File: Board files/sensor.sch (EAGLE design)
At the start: 33 parts, among them Q1 BCM847DS, U1 TL974, U2 TL974

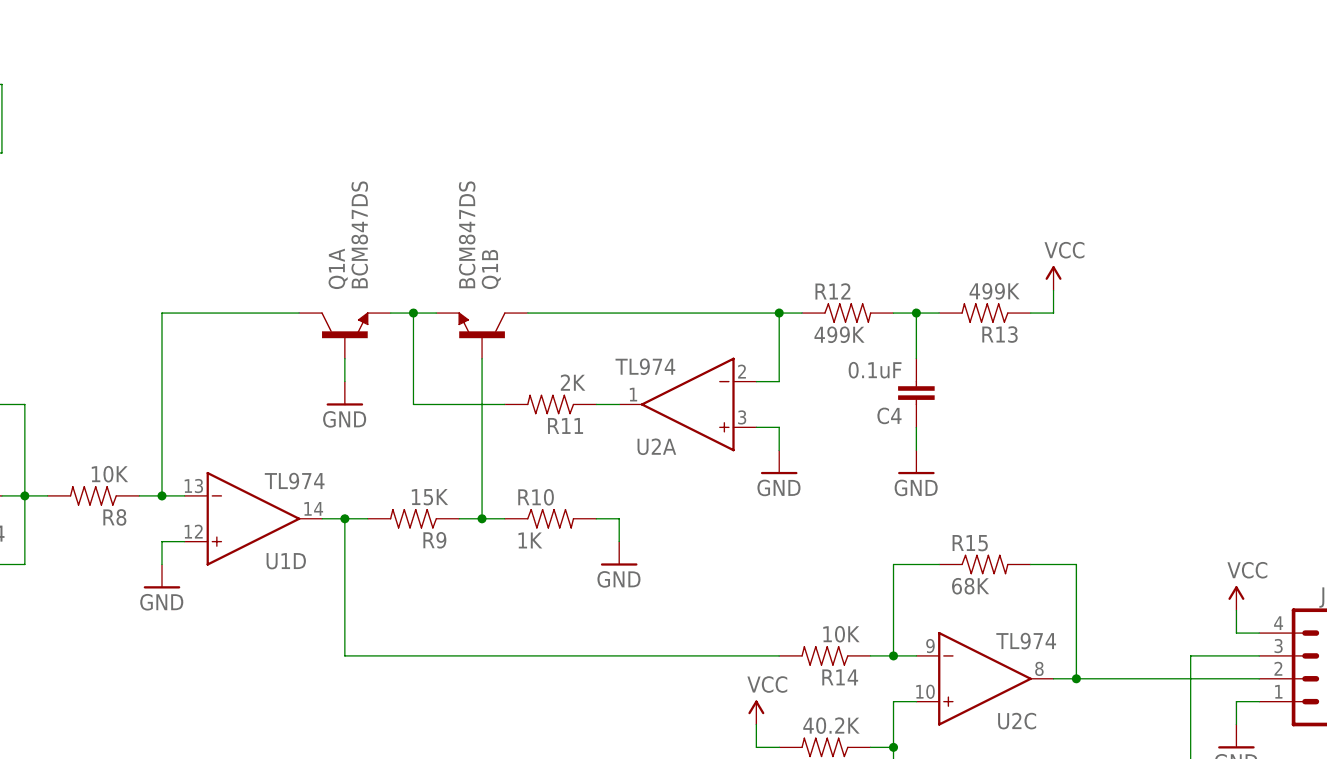
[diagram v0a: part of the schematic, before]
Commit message: Fixed sensor board bug
Added a capacitor between U1p13 and U1p14
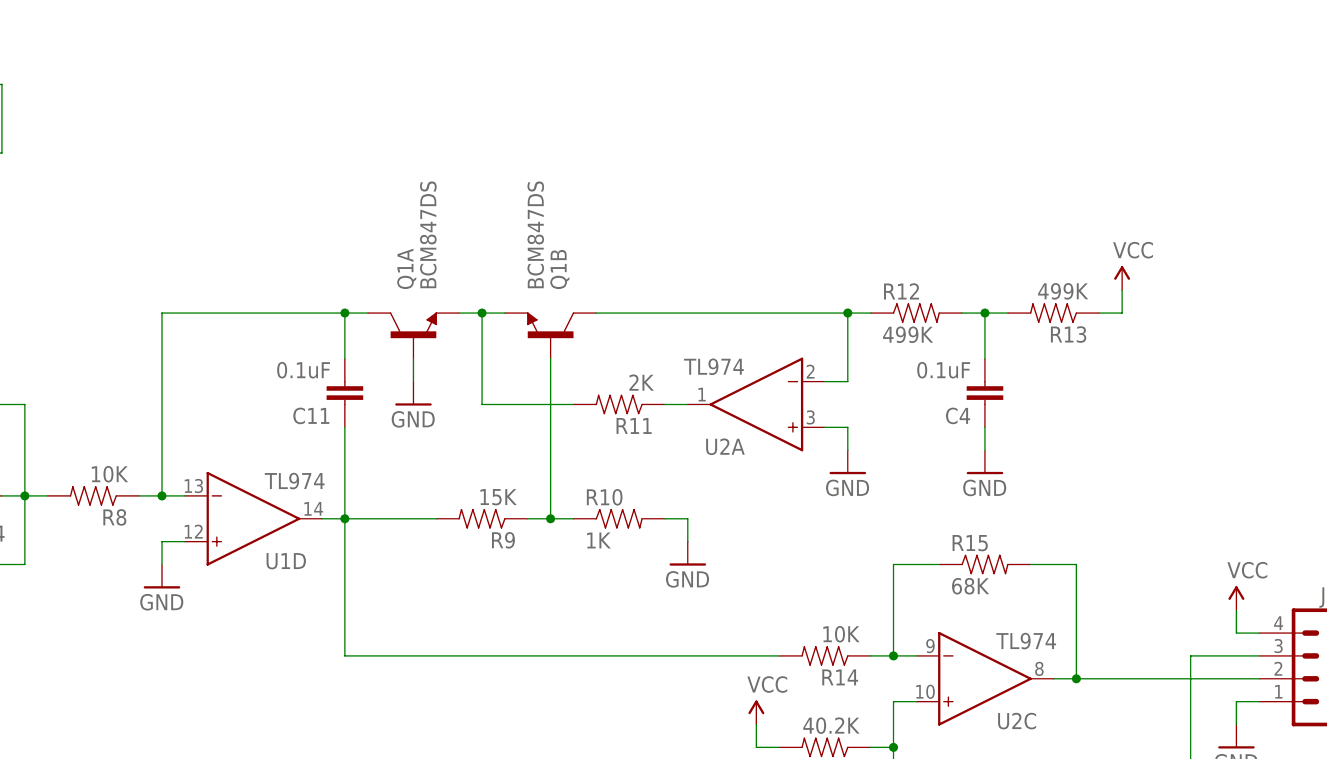
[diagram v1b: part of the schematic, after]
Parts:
- added C11: 0.1uF, SparkFun-Capacitors:CAP0805
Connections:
- net N$13: now also C11.2
- net N$17: now also C11.1
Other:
- moved on the sheet: C4, Q1A, Q1B, R10, R11, R12, R13, R9, U2A
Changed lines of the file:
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@@
 <part name="SUPPLY8" library="SparkFun-Aesthetics" deviceset="VNEG" device=""/>
 <part name="GND16" library="SparkFun-Aesthetics" deviceset="GND" device=""/>
+<part name="C11" library="SparkFun-Capacitors" deviceset="CAP" device="0805" value="0.1uF"/>
 </parts>
 <sheets>
@@
 <instance part="SUPPLY4" gate="G$2" x="17.78" y="86.36"/>
 <instance part="D1" gate="G$1" x="99.06" y="48.26" rot="MR180"/>
-<instance part="Q1" gate="A" x="205.74" y="63.5" rot="R90"/>
-<instance part="Q1" gate="B" x="220.98" y="63.5" rot="MR90"/>
+<instance part="Q1" gate="A" x="213.36" y="63.5" rot="R90"/>
+<instance part="Q1" gate="B" x="228.6" y="63.5" rot="MR90"/>
 <instance part="U1" gate="A" x="50.8" y="40.64"/>
 <instance part="U1" gate="B" x="86.36" y="38.1" rot="MR180"/>
@@
 <instance part="U1" gate="P" x="17.78" y="104.14"/>
 <instance part="U1" gate="D" x="193.04" y="43.18" rot="MR180"/>
-<instance part="U2" gate="A" x="246.38" y="55.88" rot="R180"/>
+<instance part="U2" gate="A" x="254" y="55.88" rot="R180"/>
 <instance part="U2" gate="C" x="274.32" y="25.4" rot="MR180"/>
 <instance part="U2" gate="P" x="53.34" y="104.14"/>
 <instance part="R8" gate="G$1" x="177.8" y="45.72" rot="R180"/>
-<instance part="GND2" gate="1" x="205.74" y="55.88"/>
-<instance part="R9" gate="G$1" x="213.36" y="43.18" rot="R180"/>
-<instance part="R11" gate="G$1" x="228.6" y="55.88" rot="R180"/>
-<instance part="R12" gate="G$1" x="261.62" y="66.04"/>
-<instance part="R10" gate="G$1" x="228.6" y="43.18"/>
-<instance part="GND9" gate="1" x="236.22" y="38.1"/>
-<instance part="GND10" gate="1" x="254" y="48.26"/>
-<instance part="R13" gate="G$1" x="276.86" y="66.04" rot="R180"/>
-<instance part="SUPPLY5" gate="1" x="284.48" y="68.58"/>
-<instance part="C4" gate="G$1" x="269.24" y="58.42" rot="R180"/>
-<instance part="GND11" gate="1" x="269.24" y="48.26"/>
+<instance part="GND2" gate="1" x="213.36" y="55.88"/>
+<instance part="R9" gate="G$1" x="220.98" y="43.18" rot="R180"/>
+<instance part="R11" gate="G$1" x="236.22" y="55.88" rot="R180"/>
+<instance part="R12" gate="G$1" x="269.24" y="66.04"/>
+<instance part="R10" gate="G$1" x="236.22" y="43.18"/>
+<instance part="GND9" gate="1" x="243.84" y="38.1"/>
+<instance part="GND10" gate="1" x="261.62" y="48.26"/>
+<instance part="R13" gate="G$1" x="284.48" y="66.04" rot="R180"/>
+<instance part="SUPPLY5" gate="1" x="292.1" y="68.58"/>
+<instance part="C4" gate="G$1" x="276.86" y="58.42" rot="R180"/>
+<instance part="GND11" gate="1" x="276.86" y="48.26"/>
 <instance part="R14" gate="G$1" x="259.08" y="27.94" rot="R180"/>
 <instance part="R15" gate="G$1" x="276.86" y="38.1"/>
@@
 <instance part="SUPPLY8" gate="G$2" x="104.14" y="86.36"/>
 <instance part="GND16" gate="1" x="116.84" y="96.52"/>
+<instance part="C11" gate="G$1" x="205.74" y="58.42" rot="R180"/>
 </instances>
 <busses>
@@
 <pinref part="Q1" gate="A" pin="B"/>
 <pinref part="GND2" gate="1" pin="GND"/>
-<wire x1="205.74" y1="58.42" x2="205.74" y2="60.96" width="0.1524" layer="91"/>
+<wire x1="213.36" y1="58.42" x2="213.36" y2="60.96" width="0.1524" layer="91"/>
 </segment>
 <segment>
@@
 <segment>
 <pinref part="U2" gate="A" pin="IN+"/>
-<wire x1="251.46" y1="53.34" x2="254" y2="53.34" width="0.1524" layer="91"/>
+<wire x1="259.08" y1="53.34" x2="261.62" y2="53.34" width="0.1524" layer="91"/>
 <pinref part="GND10" gate="1" pin="GND"/>
-<wire x1="254" y1="53.34" x2="254" y2="50.8" width="0.1524" layer="91"/>
+<wire x1="261.62" y1="53.34" x2="261.62" y2="50.8" width="0.1524" layer="91"/>
 </segment>
 <segment>
 <pinref part="C4" gate="G$1" pin="1"/>
 <pinref part="GND11" gate="1" pin="GND"/>
-<wire x1="269.24" y1="50.8" x2="269.24" y2="53.34" width="0.1524" layer="91"/>
+<wire x1="276.86" y1="50.8" x2="276.86" y2="53.34" width="0.1524" layer="91"/>
 </segment>
 <segment>
 <pinref part="GND9" gate="1" pin="GND"/>
 <pinref part="R10" gate="G$1" pin="2"/>
-<wire x1="236.22" y1="40.64" x2="236.22" y2="43.18" width="0.1524" layer="91"/>
-<wire x1="236.22" y1="43.18" x2="233.68" y2="43.18" width="0.1524" layer="91"/>
+<wire x1="243.84" y1="40.64" x2="243.84" y2="43.18" width="0.1524" layer="91"/>
+<wire x1="243.84" y1="43.18" x2="241.3" y2="43.18" width="0.1524" layer="91"/>
 </segment>
 <segment>
@@
 <segment>
 <pinref part="R13" gate="G$1" pin="1"/>
-<wire x1="281.94" y1="66.04" x2="284.48" y2="66.04" width="0.1524" layer="91"/>
+<wire x1="289.56" y1="66.04" x2="292.1" y2="66.04" width="0.1524" layer="91"/>
 <pinref part="SUPPLY5" gate="1" pin="VCC"/>
-<wire x1="284.48" y1="66.04" x2="284.48" y2="68.58" width="0.1524" layer="91"/>
+<wire x1="292.1" y1="66.04" x2="292.1" y2="68.58" width="0.1524" layer="91"/>
 </segment>
 <segment>
@@
 <wire x1="185.42" y1="45.72" x2="182.88" y2="45.72" width="0.1524" layer="91"/>
 <wire x1="185.42" y1="45.72" x2="185.42" y2="66.04" width="0.1524" layer="91"/>
-<wire x1="185.42" y1="66.04" x2="200.66" y2="66.04" width="0.1524" layer="91"/>
+<wire x1="185.42" y1="66.04" x2="205.74" y2="66.04" width="0.1524" layer="91"/>
 <junction x="185.42" y="45.72"/>
+<pinref part="C11" gate="G$1" pin="2"/>
+<wire x1="205.74" y1="66.04" x2="208.28" y2="66.04" width="0.1524" layer="91"/>
+<wire x1="205.74" y1="66.04" x2="205.74" y2="60.96" width="0.1524" layer="91"/>
+<junction x="205.74" y="66.04"/>
 </segment>
 </net>
@@
 <pinref part="Q1" gate="A" pin="E"/>
 <pinref part="Q1" gate="B" pin="E"/>
-<wire x1="215.9" y1="66.04" x2="213.36" y2="66.04" width="0.1524" layer="91"/>
+<wire x1="223.52" y1="66.04" x2="220.98" y2="66.04" width="0.1524" layer="91"/>
 <pinref part="R11" gate="G$1" pin="2"/>
-<wire x1="213.36" y1="66.04" x2="210.82" y2="66.04" width="0.1524" layer="91"/>
-<wire x1="213.36" y1="66.04" x2="213.36" y2="55.88" width="0.1524" layer="91"/>
-<wire x1="213.36" y1="55.88" x2="223.52" y2="55.88" width="0.1524" layer="91"/>
-<junction x="213.36" y="66.04"/>
+<wire x1="220.98" y1="66.04" x2="218.44" y2="66.04" width="0.1524" layer="91"/>
+<wire x1="220.98" y1="66.04" x2="220.98" y2="55.88" width="0.1524" layer="91"/>
+<wire x1="220.98" y1="55.88" x2="231.14" y2="55.88" width="0.1524" layer="91"/>
+<junction x="220.98" y="66.04"/>
 </segment>
 </net>
@@
 <pinref part="R11" gate="G$1" pin="1"/>
 <pinref part="U2" gate="A" pin="OUT"/>
-<wire x1="236.22" y1="55.88" x2="233.68" y2="55.88" width="0.1524" layer="91"/>
+<wire x1="243.84" y1="55.88" x2="241.3" y2="55.88" width="0.1524" layer="91"/>
 </segment>
 </net>
@@
 <pinref part="Q1" gate="B" pin="B"/>
 <pinref part="R9" gate="G$1" pin="1"/>
-<wire x1="220.98" y1="60.96" x2="220.98" y2="43.18" width="0.1524" layer="91"/>
-<wire x1="220.98" y1="43.18" x2="218.44" y2="43.18" width="0.1524" layer="91"/>
+<wire x1="228.6" y1="60.96" x2="228.6" y2="43.18" width="0.1524" layer="91"/>
+<wire x1="228.6" y1="43.18" x2="226.06" y2="43.18" width="0.1524" layer="91"/>
 <pinref part="R10" gate="G$1" pin="1"/>
-<wire x1="220.98" y1="43.18" x2="223.52" y2="43.18" width="0.1524" layer="91"/>
-<junction x="220.98" y="43.18"/>
+<wire x1="228.6" y1="43.18" x2="231.14" y2="43.18" width="0.1524" layer="91"/>
+<junction x="228.6" y="43.18"/>
 </segment>
 </net>
@@
 <pinref part="R9" gate="G$1" pin="2"/>
 <wire x1="203.2" y1="43.18" x2="205.74" y2="43.18" width="0.1524" layer="91"/>
-<wire x1="205.74" y1="43.18" x2="208.28" y2="43.18" width="0.1524" layer="91"/>
+<wire x1="205.74" y1="43.18" x2="215.9" y2="43.18" width="0.1524" layer="91"/>
 <wire x1="205.74" y1="43.18" x2="205.74" y2="27.94" width="0.1524" layer="91"/>
 <pinref part="R14" gate="G$1" pin="2"/>
 <wire x1="205.74" y1="27.94" x2="254" y2="27.94" width="0.1524" layer="91"/>
 <junction x="205.74" y="43.18"/>
+<pinref part="C11" gate="G$1" pin="1"/>
+<wire x1="205.74" y1="53.34" x2="205.74" y2="43.18" width="0.1524" layer="91"/>
 </segment>
 </net>
@@
 <segment>
 <pinref part="U2" gate="A" pin="IN-"/>
-<wire x1="251.46" y1="58.42" x2="254" y2="58.42" width="0.1524" layer="91"/>
+<wire x1="259.08" y1="58.42" x2="261.62" y2="58.42" width="0.1524" layer="91"/>
 <pinref part="Q1" gate="B" pin="C"/>
-<wire x1="254" y1="58.42" x2="254" y2="66.04" width="0.1524" layer="91"/>
-<wire x1="254" y1="66.04" x2="226.06" y2="66.04" width="0.1524" layer="91"/>
+<wire x1="261.62" y1="58.42" x2="261.62" y2="66.04" width="0.1524" layer="91"/>
+<wire x1="261.62" y1="66.04" x2="233.68" y2="66.04" width="0.1524" layer="91"/>
 <pinref part="R12" gate="G$1" pin="1"/>
-<wire x1="256.54" y1="66.04" x2="254" y2="66.04" width="0.1524" layer="91"/>
-<junction x="254" y="66.04"/>
+<wire x1="264.16" y1="66.04" x2="261.62" y2="66.04" width="0.1524" layer="91"/>
+<junction x="261.62" y="66.04"/>
 </segment>
 </net>
@@
 <pinref part="R12" gate="G$1" pin="2"/>
 <pinref part="R13" gate="G$1" pin="2"/>
-<wire x1="271.78" y1="66.04" x2="269.24" y2="66.04" width="0.1524" layer="91"/>
+<wire x1="279.4" y1="66.04" x2="276.86" y2="66.04" width="0.1524" layer="91"/>
 <pinref part="C4" gate="G$1" pin="2"/>
-<wire x1="269.24" y1="66.04" x2="266.7" y2="66.04" width="0.1524" layer="91"/>
-<wire x1="269.24" y1="60.96" x2="269.24" y2="66.04" width="0.1524" layer="91"/>
-<junction x="269.24" y="66.04"/>
-</segment>
-</net>
+<wire x1="276.86" y1="66.04" x2="274.32" y2="66.04" width="0.1524" layer="91"/>
+<wire x1="276.86" y1="60.96" x2="276.86" y2="66.04" width="0.1524" layer="91"/>
+<junction x="276.86" y="66.04"/>
+</segment>
+</net>

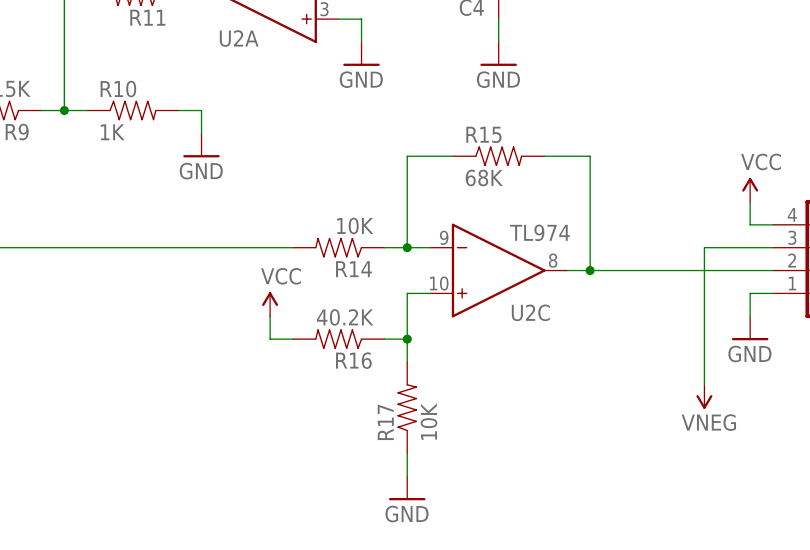
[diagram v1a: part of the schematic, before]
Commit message: Fixed level shifter resistor values
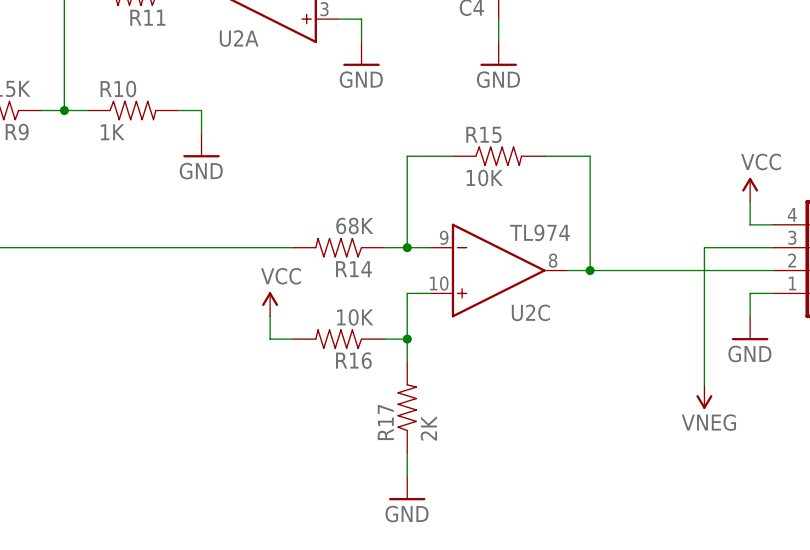
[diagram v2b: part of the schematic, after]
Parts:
- R14: value 10K -> 68K
- R15: value 68K -> 10K
- R16: value 40.2K -> 10K
- R17: value 10K -> 2K
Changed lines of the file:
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@@
 <part name="C4" library="SparkFun-Capacitors" deviceset="CAP" device="0805" value="0.1uF"/>
 <part name="GND11" library="SparkFun-Aesthetics" deviceset="GND" device=""/>
-<part name="R14" library="SparkFun-Resistors" deviceset="RESISTOR" device="0805-RES" value="10K"/>
-<part name="R15" library="SparkFun-Resistors" deviceset="RESISTOR" device="0805-RES" value="68K"/>
+<part name="R14" library="SparkFun-Resistors" deviceset="RESISTOR" device="0805-RES" value="68K"/>
+<part name="R15" library="SparkFun-Resistors" deviceset="RESISTOR" device="0805-RES" value="10K"/>
 <part name="GND13" library="SparkFun-Aesthetics" deviceset="GND" device=""/>
 <part name="SUPPLY6" library="SparkFun-Aesthetics" deviceset="VCC" device=""/>
-<part name="R16" library="SparkFun-Resistors" deviceset="RESISTOR" device="0805-RES" value="40.2K"/>
-<part name="R17" library="SparkFun-Resistors" deviceset="RESISTOR" device="0805-RES" value="10K"/>
+<part name="R16" library="SparkFun-Resistors" deviceset="RESISTOR" device="0805-RES" value="10K"/>
+<part name="R17" library="SparkFun-Resistors" deviceset="RESISTOR" device="0805-RES" value="2K"/>
 <part name="C7" library="SparkFun-Capacitors" deviceset="CAP" device="0805" value="0.1uF"/>
 <part name="C8" library="SparkFun-Capacitors" deviceset="CAP" device="0805" value="0.1uF"/>
